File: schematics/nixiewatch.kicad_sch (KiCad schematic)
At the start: 43 parts, among them Q1 BC546, Q2 IPU80R1K0CE, Q3 BC546, SW1 SW_Push, U1 NE555P, U2 TPIC6B595, U3 MCP1702-5002E/TO, U4 TPIC6B595, U5 TPIC6B595, U6 ATtiny45V-10P, U7 DS1307+, Y1 32.768kHz 12.5pF

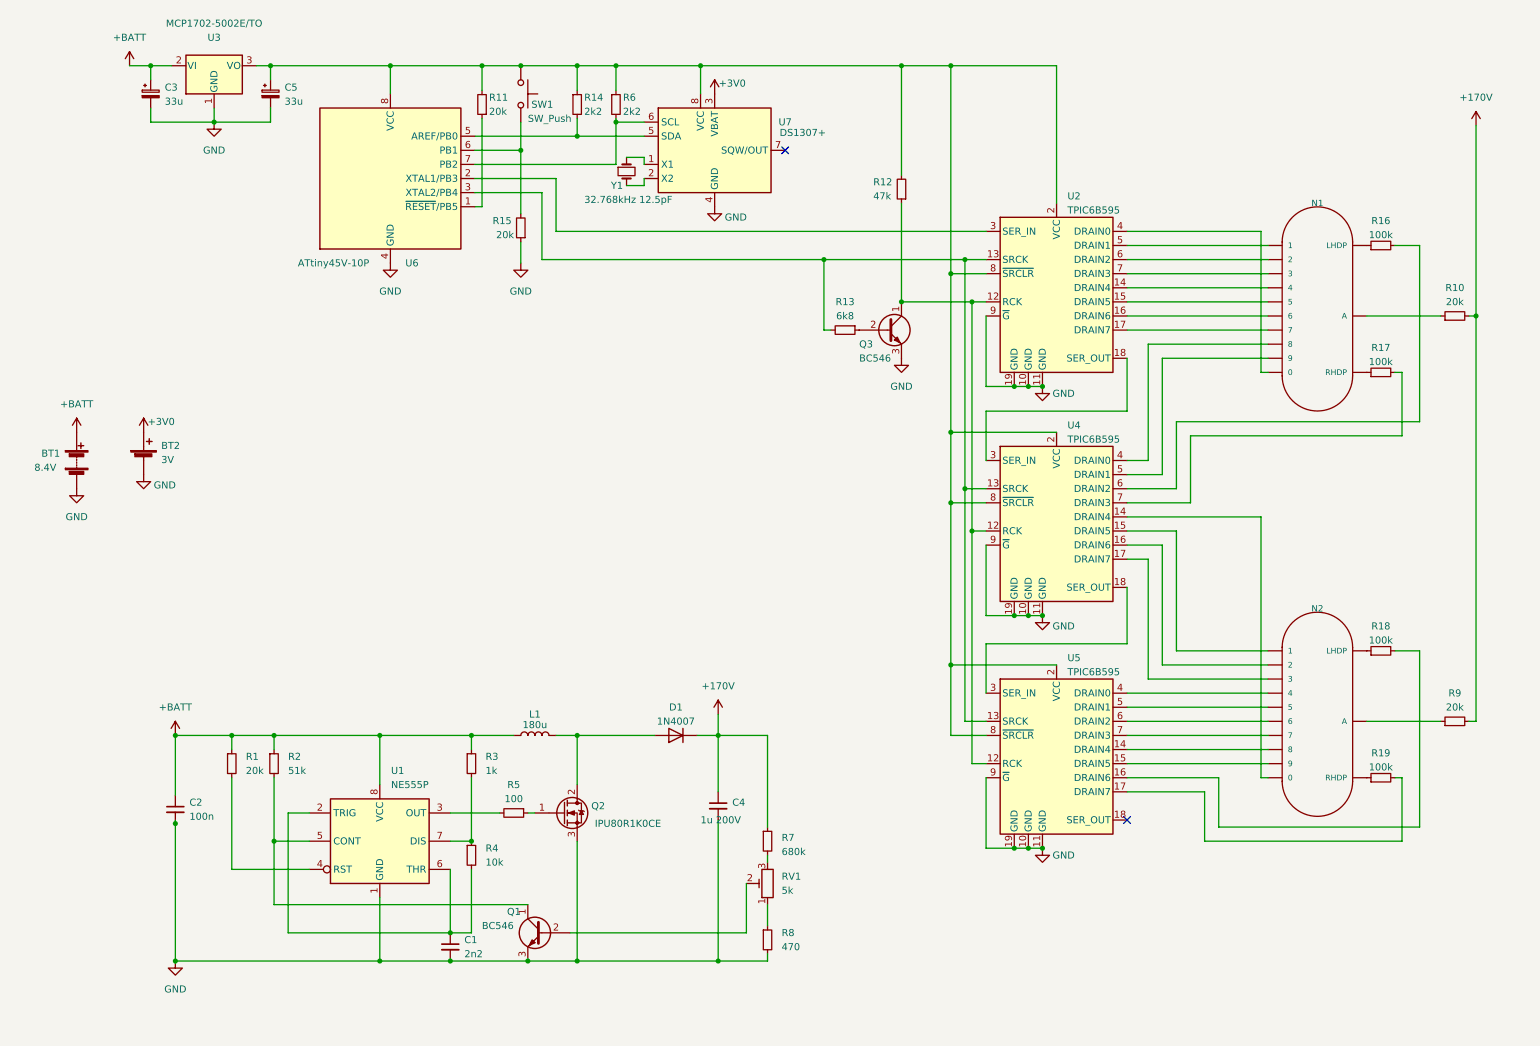
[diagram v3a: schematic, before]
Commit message: cleaned up the schematic
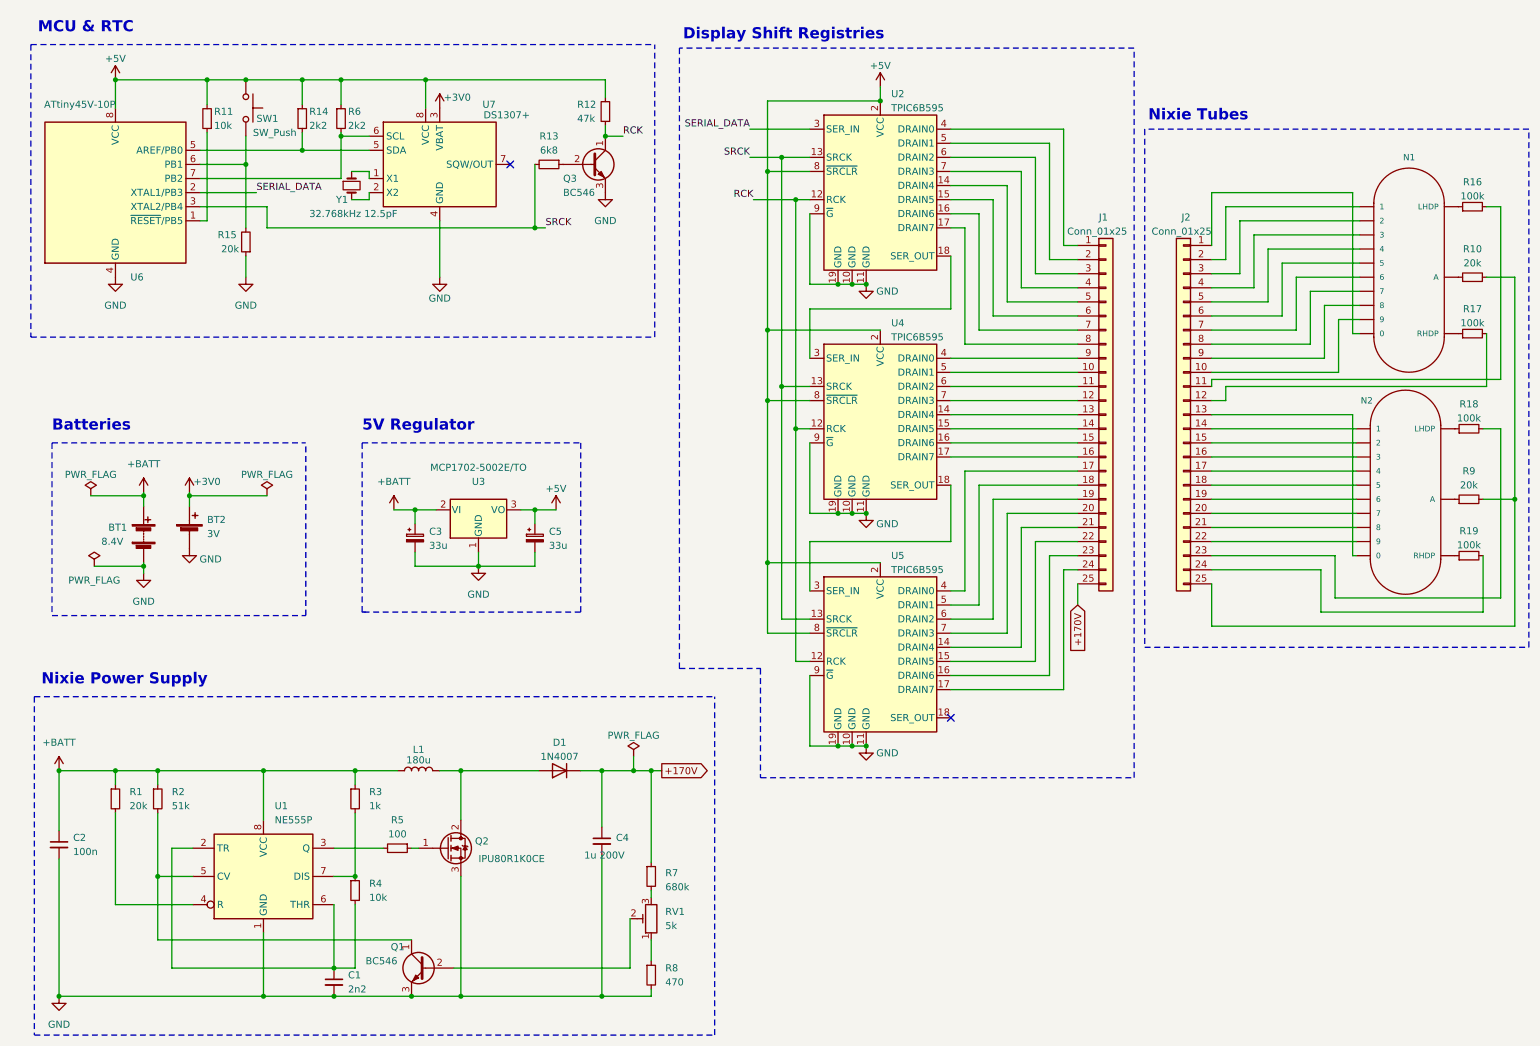
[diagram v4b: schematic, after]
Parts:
- added J1, J2: Conn_01x25, Connector_PinHeader_2.00mm:PinHeader_1x25_P2.00mm_Vertical, symbol Connector_Generic:Conn_01x25
- R11: value 20k -> 10k
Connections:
- net +170V: now also J1.25 (Pin_25); no longer R10.2, R9.2
- net +5V: now reaches C5.1, R11.2, R12.2, R14.1, R6.1, SW1.1, U2.2 (VCC), U2.8 (~{SRCLR}), U3.3 (VO), U4.2 (VCC), U4.8 (~{SRCLR}), U5.2 (VCC), U5.8 (~{SRCLR}), U6.8 (VCC), U7.8 (VCC)
- net RCK: now reaches Q3.1 (C), R12.1, U2.12 (RCK), U4.12 (RCK), U5.12 (RCK)
- net SRCK: now reaches R13.2, U2.13 (SRCK), U4.13 (SRCK), U5.13 (SRCK), U6.3 (XTAL2/PB4)
- net at U4.14 (DRAIN4): now also J1.13 (Pin_13); no longer N2.0
- net at U4.15 (DRAIN5): now also J1.14 (Pin_14); no longer N2.1
- net at U4.16 (DRAIN6): now also J1.15 (Pin_15); no longer N2.2
- net at U4.17 (DRAIN7): now also J1.16 (Pin_16); no longer N2.3
- net at U4.4 (DRAIN0): now also J1.9 (Pin_9); no longer N1.8
- net at U4.5 (DRAIN1): now also J1.10 (Pin_10); no longer N1.9
- net at U4.6 (DRAIN2): now also J1.11 (Pin_11); no longer R16.2
- net at U4.7 (DRAIN3): now also J1.12 (Pin_12); no longer R17.2
- net at N2.8: now also J2.21 (Pin_21); no longer U5.14 (DRAIN4)
- net at N2.9: now also J2.22 (Pin_22); no longer U5.15 (DRAIN5)
- net at R18.2: now also J2.23 (Pin_23); no longer U5.16 (DRAIN6)
- net at R19.2: now also J2.24 (Pin_24); no longer U5.17 (DRAIN7)
- net at N2.4: now also J2.17 (Pin_17); no longer U5.4 (DRAIN0)
- net at N2.5: now also J2.18 (Pin_18); no longer U5.5 (DRAIN1)
- net at N2.6: now also J2.19 (Pin_19); no longer U5.6 (DRAIN2)
- net at N2.7: now also J2.20 (Pin_20); no longer U5.7 (DRAIN3)
- net at N1.4: now also J2.5 (Pin_5); no longer U2.14 (DRAIN4)
- net at N1.5: now also J2.6 (Pin_6); no longer U2.15 (DRAIN5)
- net at N1.6: now also J2.7 (Pin_7); no longer U2.16 (DRAIN6)
- net at N1.7: now also J2.8 (Pin_8); no longer U2.17 (DRAIN7)
- net SERIAL_DATA: now reaches U2.3 (SER_IN), U6.2 (XTAL1/PB3)
- net at N1.0: now also J2.1 (Pin_1); no longer U2.4 (DRAIN0)
- net at N1.1: now also J2.2 (Pin_2); no longer U2.5 (DRAIN1)
- net at N1.2: now also J2.3 (Pin_3); no longer U2.6 (DRAIN2)
- net at N1.3: now also J2.4 (Pin_4); no longer U2.7 (DRAIN3)
- new net: J2.10 (Pin_10), N1.9
- new net: J2.11 (Pin_11), R16.2
- new net: J2.12 (Pin_12), R17.2
- new net: J2.13 (Pin_13), N2.0
- new net: J2.14 (Pin_14), N2.1
- new net: J2.15 (Pin_15), N2.2
- new net: J2.16 (Pin_16), N2.3
- new net: J2.25 (Pin_25), R10.2, R9.2
- new net: J2.9 (Pin_9), N1.8
- new net: J1.21 (Pin_21), U5.14 (DRAIN4)
- new net: J1.22 (Pin_22), U5.15 (DRAIN5)
- new net: J1.23 (Pin_23), U5.16 (DRAIN6)
- new net: J1.24 (Pin_24), U5.17 (DRAIN7)
- new net: J1.17 (Pin_17), U5.4 (DRAIN0)
- new net: J1.18 (Pin_18), U5.5 (DRAIN1)
- new net: J1.19 (Pin_19), U5.6 (DRAIN2)
- new net: J1.20 (Pin_20), U5.7 (DRAIN3)
- new net: J1.5 (Pin_5), U2.14 (DRAIN4)
- new net: J1.6 (Pin_6), U2.15 (DRAIN5)
- new net: J1.7 (Pin_7), U2.16 (DRAIN6)
- new net: J1.8 (Pin_8), U2.17 (DRAIN7)
- new net: J1.1 (Pin_1), U2.4 (DRAIN0)
- new net: J1.2 (Pin_2), U2.5 (DRAIN1)
- new net: J1.3 (Pin_3), U2.6 (DRAIN2)
- new net: J1.4 (Pin_4), U2.7 (DRAIN3)
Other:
- note added: "5V Regulator"
- note added: "Batteries"
- note added: "Display Shift Registries"
- note added: "MCU & RTC"
- note added: "Nixie Power Supply"
- note added: "Nixie Tubes"
- title: (none) -> Nixie Watch
- moved on the sheet: BT1, BT2, C1, C2, C3, C4, C5, D1, L1, N1, N2, Q1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

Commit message: pcb
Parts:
- removed J2: Conn_01x25, Connector_PinHeader_2.00mm:PinHeader_1x25_P2.00mm_Vertical, symbol Connector_Generic:Conn_01x25
- added H1, H2: MountingHole, MountingHole:MountingHole_2.2mm_M2, symbol Mechanical:MountingHole
- added J10: BT2_3V, Connector_PinHeader_2.00mm:PinHeader_1x01_P2.00mm_Vertical, symbol Connector_Generic:Conn_01x01
- added J2, J5: ButtonL, Connector_PinHeader_2.00mm:PinHeader_1x01_P2.00mm_Vertical, symbol Connector_Generic:Conn_01x01
- added J3: Conn_01x25, Connector_PinHeader_2.00mm:PinHeader_1x24_P2.00mm_Vertical, symbol Connector_Generic:Conn_01x24
- added J4, J6, J7, J8: ButtonH, Connector_PinHeader_2.00mm:PinHeader_1x01_P2.00mm_Vertical, symbol Connector_Generic:Conn_01x01
- added J9: BT2GND, Connector_PinHeader_2.00mm:PinHeader_1x01_P2.00mm_Vertical, symbol Connector_Generic:Conn_01x01
- BT1: footprint Connector_PinHeader_2.00mm:PinHeader_1x01_P2.00mm_Vertical -> Connector_PinHeader_2.00mm:PinHeader_1x02_P2.00mm_Vertical
- BT2: footprint Connector_PinHeader_2.00mm:PinHeader_1x01_P2.00mm_Vertical -> (none)
- J1: footprint Connector_PinHeader_2.00mm:PinHeader_1x25_P2.00mm_Vertical -> Connector_PinHeader_2.00mm:PinHeader_1x24_P2.00mm_Vertical; symbol Connector_Generic:Conn_01x25 -> Connector_Generic:Conn_01x24
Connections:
- net +170V: now also J7.1 (Pin_1); no longer J1.25 (Pin_25)
- net +3V0: now also J10.1 (Pin_1)
- net +5V: now also J4.1 (Pin_1); no longer SW1.1
- net GND: now also J9.1 (Pin_1)
- net at R15.2, U6.6 (PB1): now also J2.1 (Pin_1); no longer SW1.2
- net at N1.0: now also J3.1 (Pin_1)
- net at N1.9: now also J3.10 (Pin_10)
- net at R16.2: now also J3.11 (Pin_11)
- net at R17.2: now also J3.12 (Pin_12)
- net at N2.0: now also J3.13 (Pin_13)
- net at N2.1: now also J3.14 (Pin_14)
- net at N2.2: now also J3.15 (Pin_15)
- net at N2.3: now also J3.16 (Pin_16)
- net at N2.4: now also J3.17 (Pin_17)
- net at N2.5: now also J3.18 (Pin_18)
- net at N2.6: now also J3.19 (Pin_19)
- net at N1.1: now also J3.2 (Pin_2)
- net at N2.7: now also J3.20 (Pin_20)
- net at N2.8: now also J3.21 (Pin_21)
- net at N2.9: now also J3.22 (Pin_22)
- net at R18.2: now also J3.23 (Pin_23)
- net at R19.2: now also J3.24 (Pin_24)
- net at R10.2, R9.2: now also J8.1 (Pin_1)
- net at N1.2: now also J3.3 (Pin_3)
- net at N1.3: now also J3.4 (Pin_4)
- net at N1.4: now also J3.5 (Pin_5)
- net at N1.5: now also J3.6 (Pin_6)
- net at N1.6: now also J3.7 (Pin_7)
- net at N1.7: now also J3.8 (Pin_8)
- net at N1.8: now also J3.9 (Pin_9)
- net 170V_int: now reaches D1.2 (A), L1.2, Q2.2 (D)
- new net: J6.1 (Pin_1), SW1.1
- new net: J5.1 (Pin_1), SW1.2
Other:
- note added: "Button Not on the PCB"
- note added: "Mounting Holes"
- note added: "Nixie Tubes Not on the PCB"
- note removed: "Nixie Tubes"
- moved on the sheet: BT1, BT2, C3, C5, U3

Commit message: smd version
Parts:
- removed D1: 1N4007, Diode_THT:D_DO-41_SOD81_P10.16mm_Horizontal, symbol Diode:1N4007
- removed J1: Conn_01x25, Connector_PinHeader_2.00mm:PinHeader_1x24_P2.00mm_Vertical, symbol Connector_Generic:Conn_01x24
- removed Q1, Q3: BC546, Package_TO_SOT_THT:TO-92_Inline, symbol Transistor_BJT:BC546
- removed U1: NE555P, Package_DIP:DIP-8_W7.62mm, symbol Timer:NE555P
- removed U2, U4, U5: TPIC6B595, Package_DIP:DIP-20_W7.62mm, symbol my_library:TPIC6B595
- removed U6: ATtiny45V-10P, Package_DIP:DIP-8_W7.62mm, symbol MCU_Microchip_ATtiny:ATtiny45V-10P
- removed U7: DS1307+, Package_DIP:DIP-8_W7.62mm, symbol Timer_RTC:DS1307+
- added D1: S1K, Diode_SMD:D_SMA_Handsoldering, symbol PCM_Diode_AKL:S1K
- added J11, J13: Conn_01x05, Connector_PinHeader_2.54mm:PinHeader_1x05_P2.54mm_Vertical, symbol Connector_Generic:Conn_01x05
- added J12: BTGND, Connector_PinHeader_2.54mm:PinHeader_1x01_P2.54mm_Vertical, symbol Connector_Generic:Conn_01x01
- added J14: Conn_01x04, Connector_PinHeader_2.54mm:PinHeader_1x04_P2.54mm_Vertical, symbol Connector_Generic:Conn_01x04
- added J15: BT1_8V, Connector_PinHeader_2.54mm:PinHeader_1x01_P2.54mm_Vertical, symbol Connector_Generic:Conn_01x01
- added J3: Conn_01x10, Connector_PinHeader_2.54mm:PinHeader_1x10_P2.54mm_Vertical, symbol Connector_Generic:Conn_01x10
- added Q1, Q3: BC846A, PCM_Package_TO_SOT_SMD_AKL:SOT-23_Handsoldering, symbol PCM_Transistor_BJT_AKL:BC846A
- added U1: DS1307Z+, Package_SO:SOIC-8_3.9x4.9mm_P1.27mm, symbol Timer_RTC:DS1307Z+
- added U2, U4, U6: TPIC6A595DWR, Package_SO:SOIC-24W_7.5x15.4mm_P1.27mm, symbol my_library:TPIC6A595DWR
- added U3: ATtiny412-SS, Package_SO:SOIC-8_3.9x4.9mm_P1.27mm, symbol MCU_Microchip_ATtiny:ATtiny412-SS
- added U7: NE555D, Package_SO:SOIC-8_3.9x4.9mm_P1.27mm, symbol Timer:NE555D
- BT1: footprint Connector_PinHeader_2.00mm:PinHeader_1x02_P2.00mm_Vertical -> Connector_PinHeader_2.54mm:PinHeader_1x02_P2.54mm_Vertical
- C1: renamed from C3; footprint Capacitor_THT:CP_Radial_D4.0mm_P1.50mm -> Capacitor_SMD:CP_Elec_5x5.3
- C2: renamed from C5; footprint Capacitor_THT:CP_Radial_D4.0mm_P1.50mm -> Capacitor_SMD:CP_Elec_5x5.3
- C3: renamed from C4; footprint Capacitor_THT:CP_Radial_D5.0mm_P2.50mm -> Library:CP_RADIAL_D5.00mm_P2.50mm_H12.0mm_Horizontal
- C4: renamed from C2; footprint Capacitor_THT:C_Disc_D3.0mm_W2.0mm_P2.50mm -> Capacitor_SMD:C_0201_0603Metric_Pad0.64x0.40mm_HandSolder
- C5: renamed from C1; value 2n2 -> 2n4; footprint Capacitor_THT:C_Disc_D3.0mm_W2.0mm_P2.50mm -> Capacitor_SMD:C_0603_1608Metric_Pad1.08x0.95mm_HandSolder
- J1: renamed from J4; footprint Connector_PinHeader_2.00mm:PinHeader_1x01_P2.00mm_Vertical -> Connector_PinHeader_2.54mm:PinHeader_1x01_P2.54mm_Vertical
- J2: footprint Connector_PinHeader_2.00mm:PinHeader_1x01_P2.00mm_Vertical -> Connector_PinHeader_2.54mm:PinHeader_1x01_P2.54mm_Vertical
- J6: renamed from J10; footprint Connector_PinHeader_2.00mm:PinHeader_1x01_P2.00mm_Vertical -> Connector_PinHeader_2.54mm:PinHeader_1x01_P2.54mm_Vertical
- J7: renamed from J9; footprint Connector_PinHeader_2.00mm:PinHeader_1x01_P2.00mm_Vertical -> Connector_PinHeader_2.54mm:PinHeader_1x01_P2.54mm_Vertical
- J9: renamed from J7; footprint Connector_PinHeader_2.00mm:PinHeader_1x01_P2.00mm_Vertical -> Connector_PinHeader_2.54mm:PinHeader_1x01_P2.54mm_Vertical
- L1: footprint Inductor_THT:L_Radial_D12.0mm_P5.00mm_Neosid_SD12k_style2 -> Inductor_SMD:L_12x12mm_H8mm
- Q2: value IPU80R1K0CE -> WMO10N60C2; footprint Package_TO_SOT_THT:SIPAK-1EP_Horizontal_TabDown -> PCM_Package_TO_SOT_SMD_AKL:TO-252-2
- R1: renamed from R12; value 47k -> 51k; footprint Resistor_THT:R_Axial_DIN0207_L6.3mm_D2.5mm_P7.62mm_Horizontal -> Resistor_SMD:R_0603_1608Metric_Pad0.98x0.95mm_HandSolder
- R13: renamed from R1; footprint Resistor_THT:R_Axial_DIN0207_L6.3mm_D2.5mm_P7.62mm_Horizontal -> Resistor_SMD:R_0201_0603Metric_Pad0.64x0.40mm_HandSolder
- R14: renamed from R2; footprint Resistor_THT:R_Axial_DIN0207_L6.3mm_D2.5mm_P7.62mm_Horizontal -> Resistor_SMD:R_0603_1608Metric_Pad0.98x0.95mm_HandSolder
- R15: renamed from R3; footprint Resistor_THT:R_Axial_DIN0207_L6.3mm_D2.5mm_P7.62mm_Horizontal -> Resistor_SMD:R_0402_1005Metric_Pad0.72x0.64mm_HandSolder
- R16: renamed from R5; footprint Resistor_THT:R_Axial_DIN0207_L6.3mm_D2.5mm_P7.62mm_Horizontal -> Resistor_SMD:R_0402_1005Metric_Pad0.72x0.64mm_HandSolder
- R17: renamed from R7; footprint Resistor_THT:R_Axial_DIN0207_L6.3mm_D2.5mm_P7.62mm_Horizontal -> Resistor_SMD:R_0603_1608Metric_Pad0.98x0.95mm_HandSolder
- R18: renamed from R4; footprint Resistor_THT:R_Axial_DIN0207_L6.3mm_D2.5mm_P7.62mm_Horizontal -> Resistor_SMD:R_0402_1005Metric_Pad0.72x0.64mm_HandSolder
- R19: renamed from R8; footprint Resistor_THT:R_Axial_DIN0207_L6.3mm_D2.5mm_P7.62mm_Horizontal -> Resistor_SMD:R_0402_1005Metric_Pad0.72x0.64mm_HandSolder
- R2: renamed from R11; value 10k -> 20k; footprint Resistor_THT:R_Axial_DIN0207_L6.3mm_D2.5mm_P7.62mm_Horizontal -> Resistor_SMD:R_0201_0603Metric_Pad0.64x0.40mm_HandSolder
- R3: renamed from R14; footprint Resistor_THT:R_Axial_DIN0207_L6.3mm_D2.5mm_P7.62mm_Horizontal -> Resistor_SMD:R_0402_1005Metric_Pad0.72x0.64mm_HandSolder
- R4: renamed from R6; footprint Resistor_THT:R_Axial_DIN0207_L6.3mm_D2.5mm_P7.62mm_Horizontal -> Resistor_SMD:R_0402_1005Metric_Pad0.72x0.64mm_HandSolder
- R5: renamed from R13; footprint Resistor_THT:R_Axial_DIN0207_L6.3mm_D2.5mm_P7.62mm_Horizontal -> Resistor_SMD:R_0402_1005Metric_Pad0.72x0.64mm_HandSolder
- R7: renamed from R15; footprint Resistor_THT:R_Axial_DIN0207_L6.3mm_D2.5mm_P7.62mm_Horizontal -> Resistor_SMD:R_0201_0603Metric_Pad0.64x0.40mm_HandSolder
- RV1: footprint Potentiometer_THT:Potentiometer_Piher_PT-6-V_Vertical -> Potentiometer_SMD:Potentiometer_ACP_CA6-VSMD_Vertical
- U5: renamed from U3; value MCP1702-5002E/TO -> DI78M05UAB; footprint Package_TO_SOT_THT:TO-92_Inline -> Package_TO_SOT_SMD:SOT-89-3_Handsoldering
- renumbered J8 to J10, J3 to J4, J6 to J5, J5 to J8, R18 to R10, R9 to R11, R19 to R12, R16 to R6, R10 to R8, R17 to R9
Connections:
- net +170V: now also D1.1 (K)
- net +3V0: now also U1.3 (VBAT)
- net +5V: now also U5.1 (VO), U1.8 (VCC), U2.21 (VCC), U2.3 (~{SRCLR}), U3.1 (VCC), U4.21 (VCC), U4.3 (~{SRCLR}), U6.21 (VCC), U6.3 (~{SRCLR}); no longer U5.3 (VO)
- net +BATT: now also U5.3 (VI), J15.1 (Pin_1), U7.8 (VCC); no longer U5.2 (VI)
- net 170V_int: now also D1.2 (A)
- net GND: now also U5.2 (GND), J12.1 (Pin_1), Q1.2 (E), Q3.2 (E), U1.4 (GND), U2.16 (LGND), U2.17 (PGND), U2.18 (PGND), U2.19 (PGND), U2.20 (PGND), U2.4 (~{G}), U2.5 (PGND), U2.6 (PGND), U2.7 (PGND), U2.8 (PGND), U3.8 (GND), U4.16 (LGND), U4.17 (PGND), U4.18 (PGND), U4.19 (PGND), U4.20 (PGND), U4.4 (~{G}), U4.5 (PGND), U4.6 (PGND), U4.7 (PGND), U4.8 (PGND), U6.16 (LGND), U6.17 (PGND), U6.18 (PGND), U6.19 (PGND), U6.20 (PGND), U6.4 (~{G}), U6.5 (PGND), U6.6 (PGND), U6.7 (PGND), U6.8 (PGND), U7.1 (GND); no longer U5.1 (GND)
- net RCK: now also Q1.3 (C), U2.9 (RCK), U4.9 (RCK), U6.9 (RCK)
- net SERIAL_DATA: now also U2.22 (SER_IN), U3.7 (PA3)
- net SRCK: now also U2.10 (SRCK), U3.2 (PA6), U4.10 (SRCK), U6.10 (SRCK)
- net at R13.2: now also U7.4 (R)
- net at J2.1 (Pin_1), R7.2: now also U3.3 (PA7)
- net at R14.2: now also Q3.3 (C), U7.5 (CV)
- net at Y1.1: now also U1.1 (X1)
- net at Y1.2: now also U1.2 (X2)
- net at R3.2: now also U1.5 (SDA), U3.4 (PA1)
- net at R4.2: now also U1.6 (SCL), U3.5 (PA2)
- net at R2.1: now also U3.6 (~{RESET}/PA0)
- net at C5.1, R18.2: now also U7.2 (TR), U7.6 (THR)
- net at R5.1: now also Q1.1 (B)
- net at RV1.2: now also Q3.1 (B)
- net at R16.2: now also U7.3 (Q)
- net at R15.2, R18.1: now also U7.7 (DIS)
- new net: J3.1 (Pin_1), U2.12 (DRAIN5)
- new net: J3.10 (Pin_10), U4.13 (DRAIN6)
- new net: J3.2 (Pin_2), U2.13 (DRAIN6)
- new net: J3.3 (Pin_3), U2.14 (DRAIN7)
- new net: J3.4 (Pin_4), U4.23 (DRAIN0)
- new net: J3.5 (Pin_5), U4.24 (DRAIN1)
- new net: J3.6 (Pin_6), U4.1 (DRAIN2)
- new net: J3.7 (Pin_7), U4.2 (DRAIN3)
- new net: J3.8 (Pin_8), U4.11 (DRAIN4)
- new net: J3.9 (Pin_9), U4.12 (DRAIN5)
- new net: J11.3 (Pin_3), U2.1 (DRAIN2)
- new net: J11.5 (Pin_5), U2.11 (DRAIN4)
- new net: U2.15 (SER_OUT), U4.22 (SER_IN)
- new net: J11.4 (Pin_4), U2.2 (DRAIN3)
- new net: J11.1 (Pin_1), U2.23 (DRAIN0)
- new net: J11.2 (Pin_2), U2.24 (DRAIN1)
- new net: J14.4 (Pin_4), U6.1 (DRAIN2)
- new net: J13.2 (Pin_2), U6.11 (DRAIN4)
- new net: J13.3 (Pin_3), U6.12 (DRAIN5)
- new net: J13.4 (Pin_4), U6.13 (DRAIN6)
- new net: J13.5 (Pin_5), U6.14 (DRAIN7)
- new net: J13.1 (Pin_1), U6.2 (DRAIN3)
- new net: U4.15 (SER_OUT), U6.22 (SER_IN)
- new net: J14.2 (Pin_2), U6.23 (DRAIN0)
- new net: J14.3 (Pin_3), U6.24 (DRAIN1)
- new net: J14.1 (Pin_1), U4.14 (DRAIN7)

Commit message: update
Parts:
- removed H1, H2: MountingHole, MountingHole:MountingHole_2.2mm_M2, symbol Mechanical:MountingHole
- added J16: reset, Connector_PinHeader_1.00mm:PinHeader_1x01_P1.00mm_Vertical, symbol Connector_Generic:Conn_01x01
- added J17: mosi, Connector_PinHeader_1.00mm:PinHeader_1x01_P1.00mm_Vertical, symbol Connector_Generic:Conn_01x01
- added J18: miso, Connector_PinHeader_1.00mm:PinHeader_1x01_P1.00mm_Vertical, symbol Connector_Generic:Conn_01x01
- added J19: sck, Connector_PinHeader_1.00mm:PinHeader_1x01_P1.00mm_Vertical, symbol Connector_Generic:Conn_01x01
- C5: value 2n4 -> 2n2; footprint Capacitor_SMD:C_0603_1608Metric_Pad1.08x0.95mm_HandSolder -> Capacitor_SMD:C_0201_0603Metric_Pad0.64x0.40mm_HandSolder
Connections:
- net SERIAL_DATA: now also J19.1 (Pin_1)
- net at R2.1, U3.6 (~{RESET}/PA0): now also J16.1 (Pin_1)
- net at R3.2, U1.5 (SDA), U3.4 (PA1): now also J17.1 (Pin_1)
- net at R4.2, U1.6 (SCL), U3.5 (PA2): now also J18.1 (Pin_1)
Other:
- note removed: "Mounting Holes"
- moved on the sheet: J1, J2, Q1, R1, R2, R5, R7, U1, U3, Y1
